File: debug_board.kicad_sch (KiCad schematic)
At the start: 21 parts, among them IC1 FT232HL-REEL, J1 USB_C_Receptacle, U1 LT1963AxST-3.3, U2 USB2514B_Bi, Y1 ABLS-24.000MHZ-B4-T

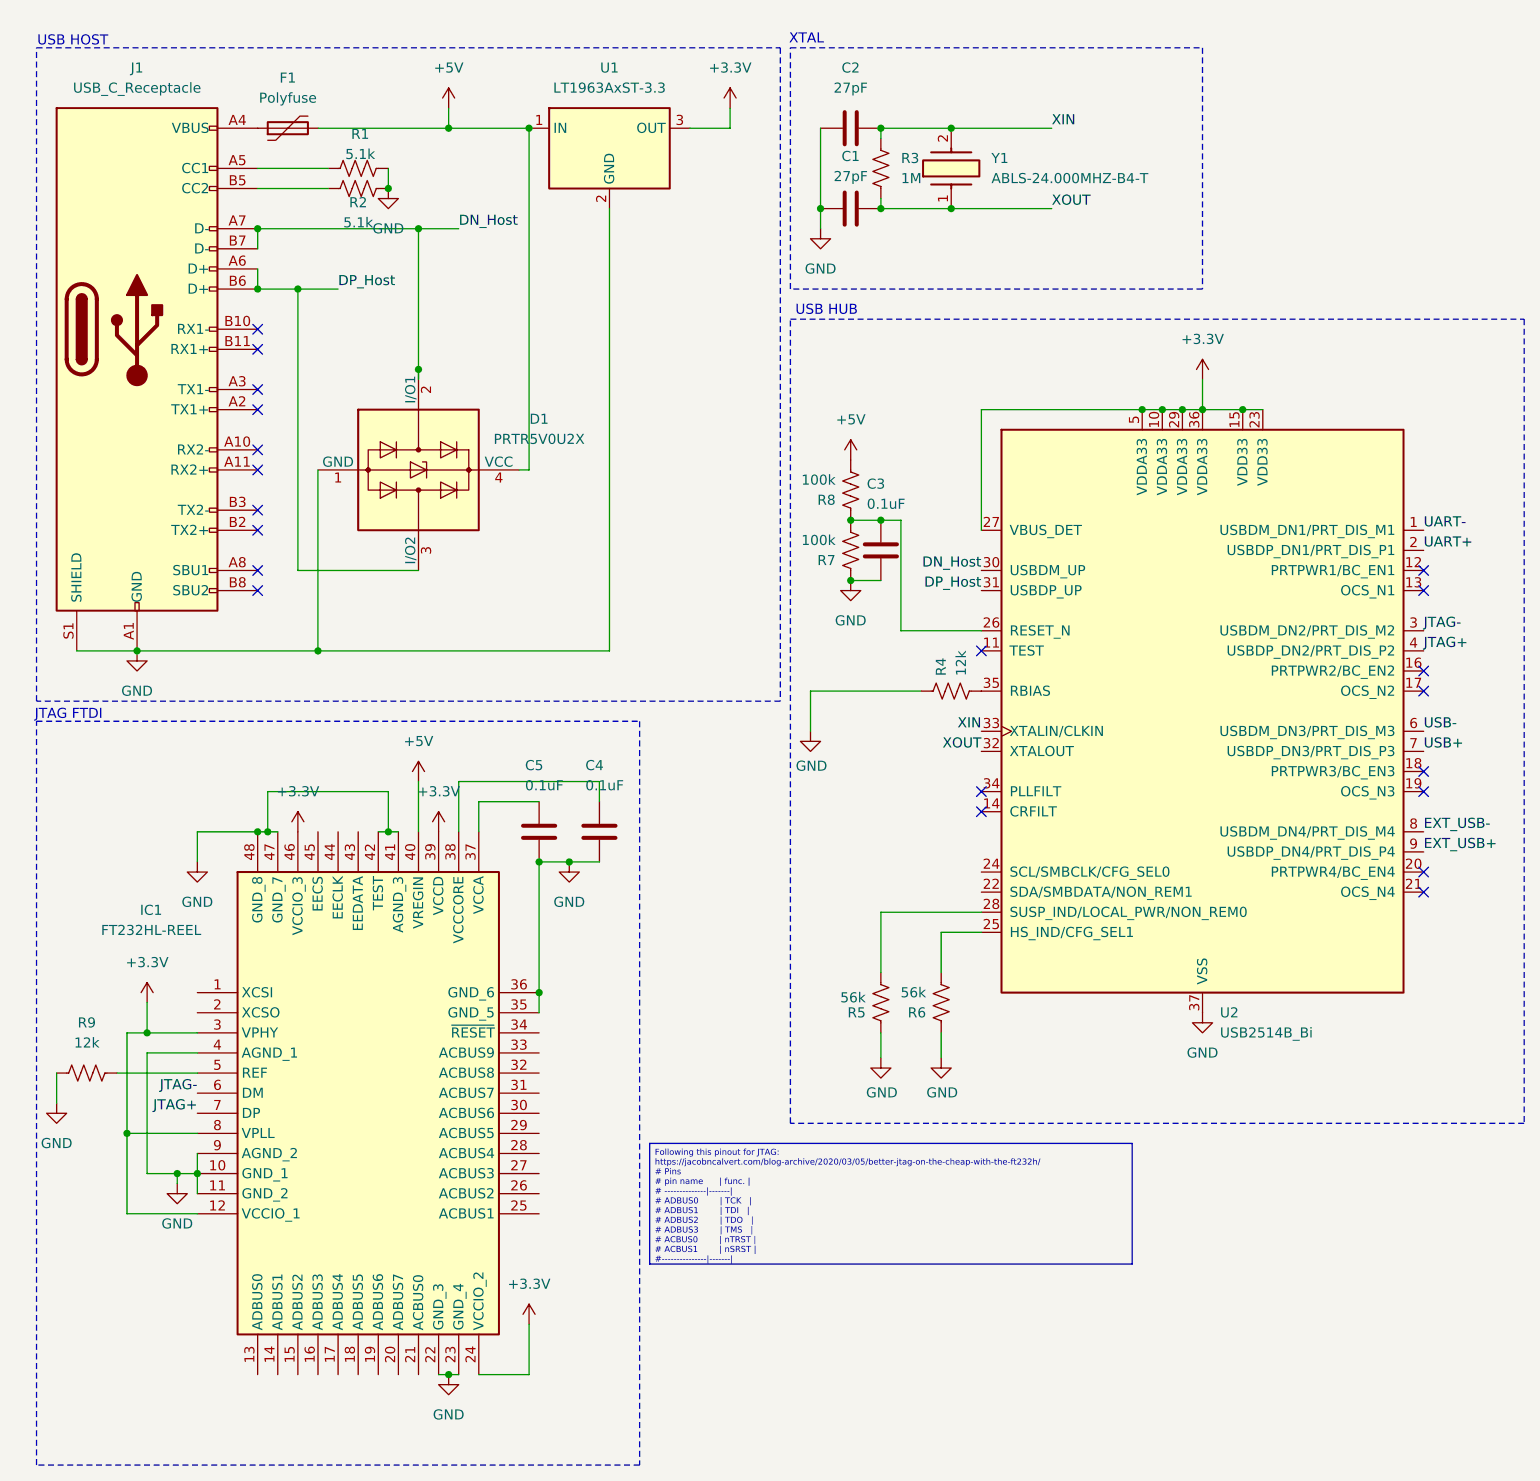
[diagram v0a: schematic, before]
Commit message: changed upstream usb to not power hub. Will add PD usb source later
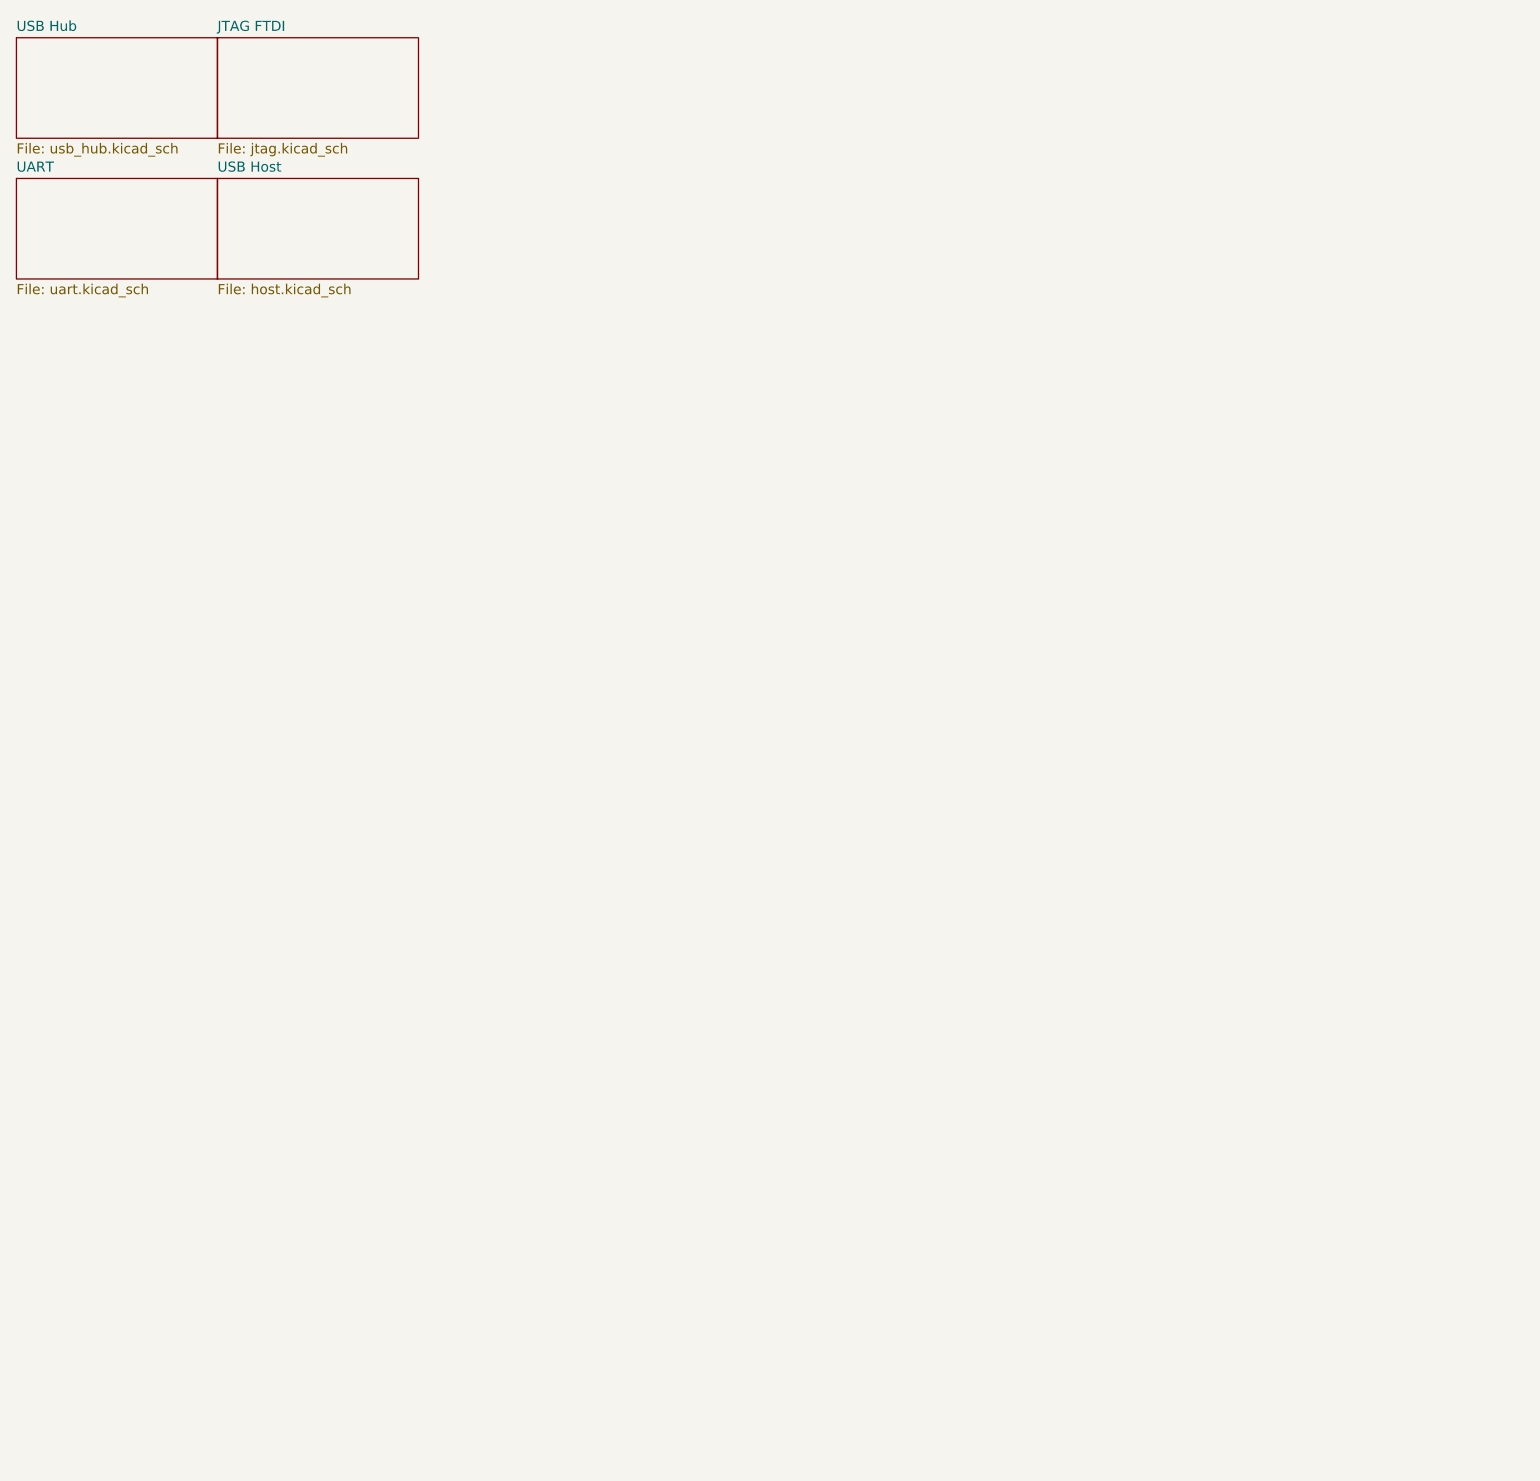
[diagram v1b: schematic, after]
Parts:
- removed C1, C2: 27pF, symbol Device:C
- removed C3, C4, C5: 0.1uF, symbol Device:C
- removed D1: PRTR5V0U2X, Package_TO_SOT_SMD:SOT-143, symbol Power_Protection:PRTR5V0U2X
- removed F1: Polyfuse, symbol Device:Polyfuse
- removed IC1: FT232HL-REEL, QFP50P900X900X160-48N, symbol SamacSys_Parts:FT232HL-REEL
- removed J1: USB_C_Receptacle, symbol Connector:USB_C_Receptacle
- removed R1, R2: 5.1k, symbol Device:R_US
- removed R3: 1M, symbol Device:R_US
- removed R4: 12k, Resistor_SMD:R_0805_2012Metric_Pad1.15x1.40mm_HandSolder, symbol Device:R_US
- removed R5, R6: 56k, Resistor_SMD:R_0805_2012Metric_Pad1.15x1.40mm_HandSolder, symbol Device:R_US
- removed R7, R8: 100k, Resistor_SMD:R_0805_2012Metric_Pad1.15x1.40mm_HandSolder, symbol Device:R_US
- removed R9: 12k, symbol Device:R_US
- removed U1: LT1963AxST-3.3, Package_TO_SOT_SMD:SOT-223-3_TabPin2, symbol Regulator_Linear:LT1963AxST-3.3
- removed U2: USB2514B_Bi, Package_DFN_QFN:QFN-36-1EP_6x6mm_P0.5mm_EP3.7x3.7mm, symbol Interface_USB:USB2514B_Bi
- removed Y1: ABLS-24.000MHZ-B4-T, ABLS24000MHZB4T, symbol SamacSys_Parts:ABLS-24.000MHZ-B4-T
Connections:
- no-connect marks 21 -> 0
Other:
- added sheet JTAG FTDI (jtag.kicad_sch)
- added sheet UART (uart.kicad_sch)
- added sheet USB Host (host.kicad_sch)
- added sheet USB Hub (usb_hub.kicad_sch)
- note removed: "JTAG FTDI"
- note removed: "USB HOST"
- note removed: "USB HUB"
- note removed: "XTAL"

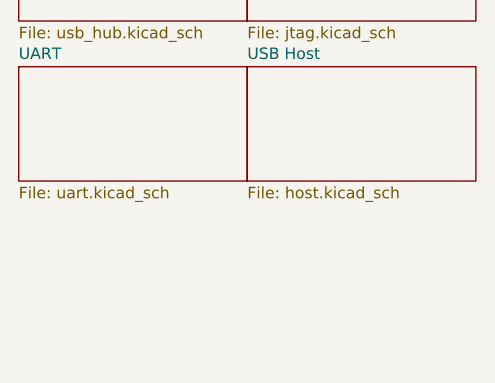
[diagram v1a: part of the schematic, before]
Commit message: Added PD, need to work on a power mux and regulator
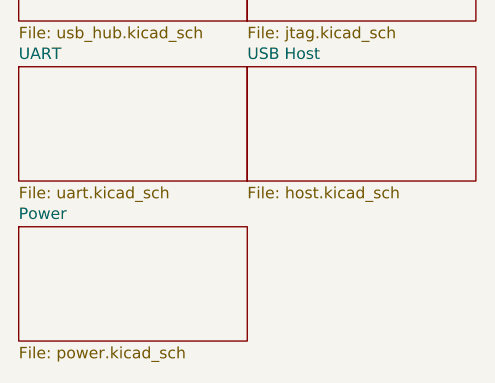
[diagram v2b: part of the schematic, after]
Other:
- added sheet Power (power.kicad_sch)
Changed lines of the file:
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@@
+	)
+	(sheet
+		(at 12.7 50.8)
+		(size 25.4 12.7)
+		(fields_autoplaced yes)
+		(stroke
+			(width 0.1524)
+			(type solid)
+		)
+		(fill
+			(color 0 0 0 0.0000)
+		)
+		(property "Sheetname" "Power"
+			(at 12.7 50.0884 0)
+			(effects
+				(font
+					(size 1.27 1.27)
+				)
+				(justify left bottom)
+			)
+		)
+		(property "Sheetfile" "power.kicad_sch"
+			(at 12.7 64.0846 0)
+			(effects
+				(font
+					(size 1.27 1.27)
+				)
+				(justify left top)
+			)
+		)
+		(instances
+			(project "debug_board"
+				(path "/9ba02813-5189-4482-9c9e-35a29bc7aded"
+					(page "6")
+				)
+			)
+		)
 	)
 	(sheet
